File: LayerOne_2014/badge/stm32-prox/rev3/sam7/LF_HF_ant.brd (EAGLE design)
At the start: 99 x 50 mm, 30 parts

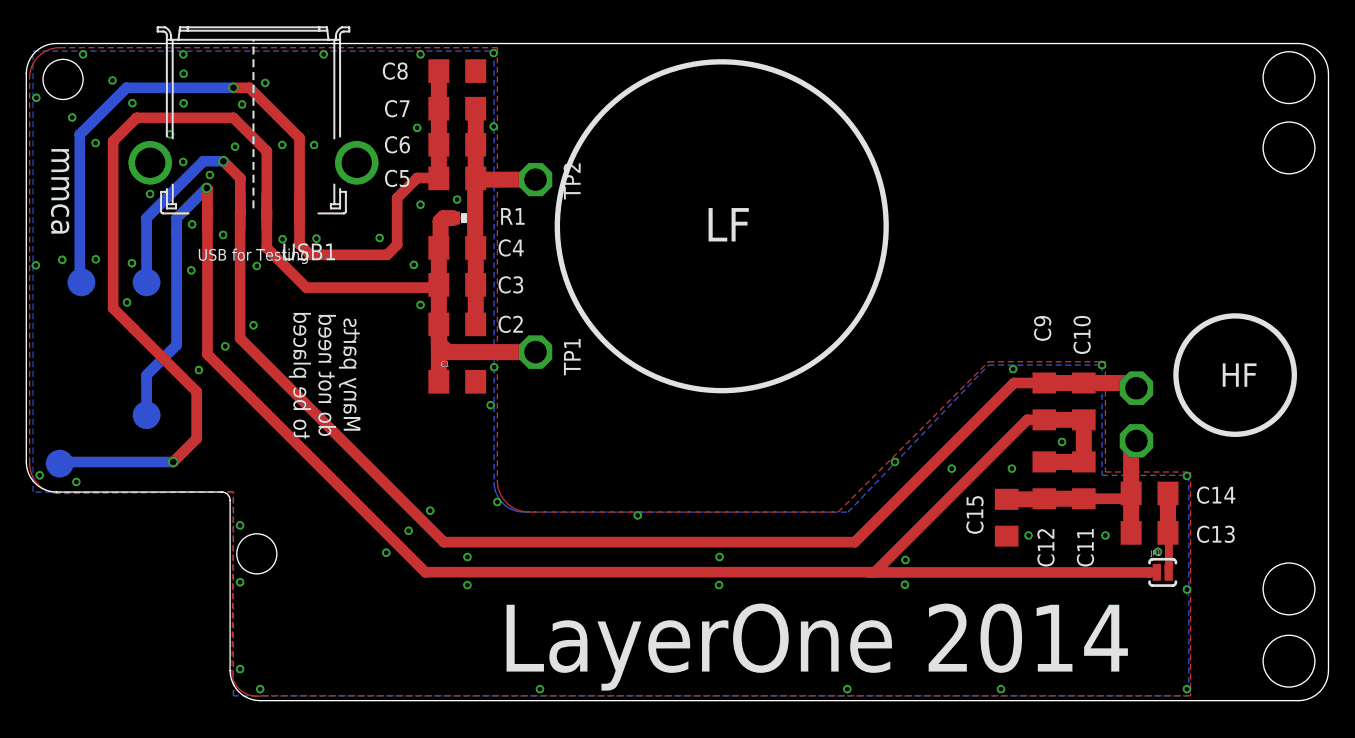
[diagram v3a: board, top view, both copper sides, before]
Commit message: 
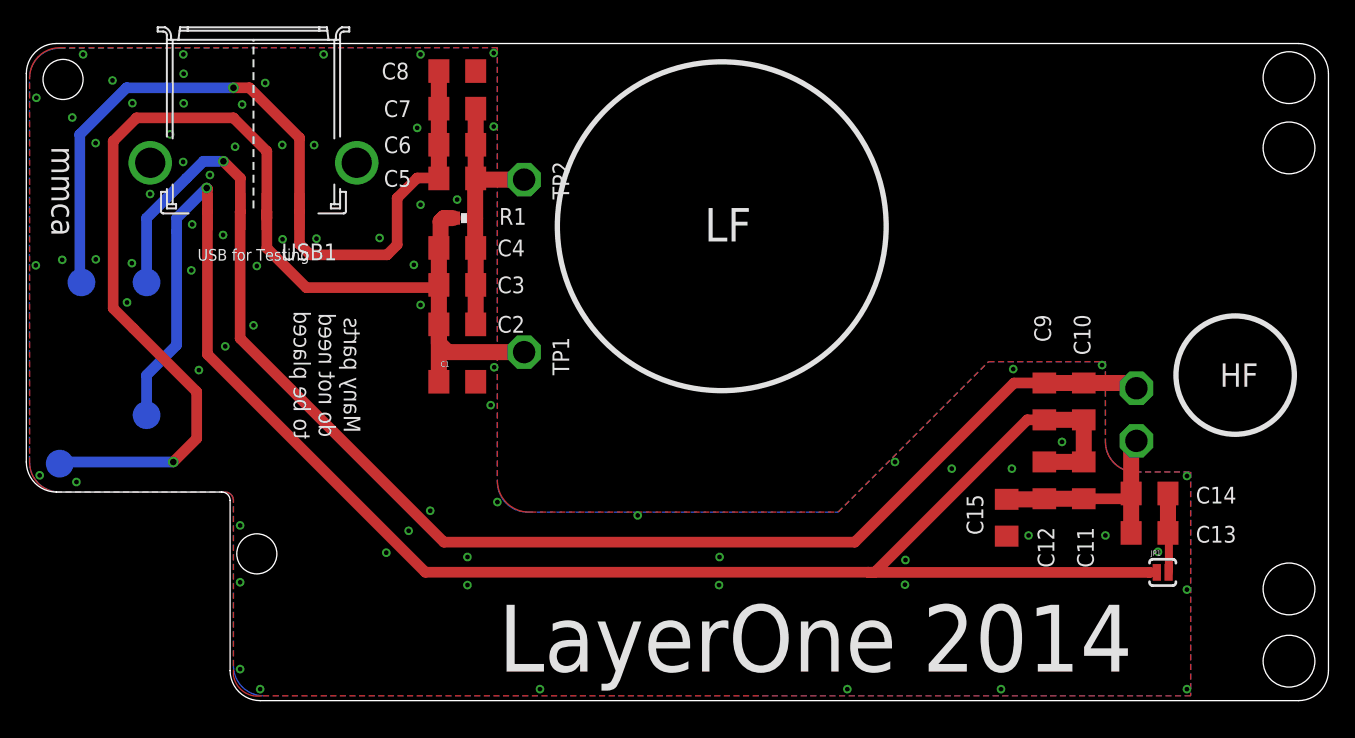
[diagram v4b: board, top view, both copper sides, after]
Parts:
- moved TP1 0.87 mm to (37.8, 1.75)
- moved TP2 0.87 mm to (37.8, 14.9)
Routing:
- net LO1: track 95.4 -> 94.5 mm
- net N$3: track 21.6 -> 20.7 mm
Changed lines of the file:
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@@
 <attribute name="VALUE" x="31.369" y="18.732" size="0.4064" layer="27"/>
 </element>
-<element name="TP1" library="testpad" package="P1-17" value="PTR1PAD1-17" x="38.716" y="1.748" smashed="yes" rot="R270">
-<attribute name="TP_SIGNAL_NAME" value="" x="35.541" y="3.018" size="1" layer="37" rot="R270"/>
-<attribute name="NAME" x="40.875" y="2.891" size="1.27" layer="25" ratio="10" rot="R270"/>
-<attribute name="VALUE" x="38.716" y="1.748" size="0.0254" layer="27" rot="R270"/>
-</element>
-<element name="TP2" library="testpad" package="P1-17" value="PTR1PAD1-17" x="38.716" y="14.86" smashed="yes" rot="R270">
-<attribute name="TP_SIGNAL_NAME" value="" x="35.541" y="16.13" size="1" layer="37" rot="R270"/>
-<attribute name="NAME" x="40.875" y="16.257" size="1.27" layer="25" ratio="10" rot="R270"/>
-<attribute name="VALUE" x="38.716" y="14.86" size="0.0254" layer="27" rot="R270"/>
+<element name="TP1" library="testpad" package="P1-17" value="PTR1PAD1-17" x="37.846" y="1.748" smashed="yes" rot="R270">
+<attribute name="TP_SIGNAL_NAME" value="" x="34.671" y="3.018" size="1" layer="37" rot="R270"/>
+<attribute name="NAME" x="40.005" y="2.891" size="1.27" layer="25" ratio="10" rot="R270"/>
+<attribute name="VALUE" x="37.846" y="1.748" size="0.0254" layer="27" rot="R270"/>
+</element>
+<element name="TP2" library="testpad" package="P1-17" value="PTR1PAD1-17" x="37.846" y="14.86" smashed="yes" rot="R270">
+<attribute name="TP_SIGNAL_NAME" value="" x="34.671" y="16.13" size="1" layer="37" rot="R270"/>
+<attribute name="NAME" x="40.005" y="16.257" size="1.27" layer="25" ratio="10" rot="R270"/>
+<attribute name="VALUE" x="37.846" y="14.86" size="0.0254" layer="27" rot="R270"/>
 </element>
 <element name="TP3" library="testpad" package="TP_MILLMAX_R" value="TP" x="2.54" y="-6.731" smashed="yes" rot="MR0">
@@
 <wire x1="18.288" y1="17.018" x2="18.288" y2="11.938" width="0.8128" layer="1"/>
 <wire x1="31.366" y1="3.858" x2="31.496" y2="3.818" width="0.8128" layer="1"/>
-<wire x1="32.034" y1="1.748" x2="38.716" y2="1.748" width="1.2192" layer="1"/>
+<wire x1="32.034" y1="1.748" x2="37.846" y2="1.748" width="1.2192" layer="1"/>
 <wire x1="8.128" y1="3.556" x2="12.954" y2="-1.27" width="0.8128" layer="1"/>
 <wire x1="12.954" y1="-1.27" x2="12.954" y2="-4.826" width="0.8128" layer="1"/>
@@
 <wire x1="34.336" y1="14.954" x2="34.166" y2="14.954" width="1.2192" layer="1"/>
 <wire x1="34.336" y1="14.954" x2="34.336" y2="14.86" width="1.2192" layer="1"/>
-<wire x1="34.336" y1="14.86" x2="38.716" y2="14.86" width="1.2192" layer="1"/>
+<wire x1="34.336" y1="14.86" x2="37.846" y2="14.86" width="1.2192" layer="1"/>
 <wire x1="34.124" y1="9.668" x2="34.166" y2="9.668" width="0.8128" layer="1"/>
 <wire x1="34.336" y1="9.572" x2="34.166" y2="9.668" width="0.8128" layer="1"/>
@@
 <signal name="GND">
 <polygon width="0.4064" layer="1">
-<vertex x="15.748" y="-8.89"/>
-<vertex x="2.5587375" y="-8.998109375" curve="-90.468374"/>
+<vertex x="15.748" y="-22.8492"/>
+<vertex x="15.748" y="-9.525" curve="90"/>
+<vertex x="15.113" y="-8.89"/>
+<vertex x="2.5587375" y="-8.89" curve="-90.468374"/>
 <vertex x="0.254" y="-6.712184375"/>
 <vertex x="0.254" y="22.606" curve="-90"/>
@@
 <vertex x="73.152" y="1.016"/>
 <vertex x="82.042" y="1.016"/>
-<vertex x="82.042" y="-7.366"/>
+<vertex x="82.042" y="-5.08" curve="90"/>
+<vertex x="84.328" y="-7.366"/>
 <vertex x="88.519" y="-7.366"/>
 <vertex x="88.519" y="-24.38398125"/>
 <vertex x="17.9179375" y="-24.384" curve="-90.274054"/>
-<vertex x="15.63894375" y="-22.8492"/>
 </polygon>
 <contactref element="C15" pad="2"/>
@@
 <via x="29.718" y="18.796" extent="1-16" drill="0.3556"/>
 <via x="35.5346" y="18.8976" extent="1-16" drill="0.3556"/>
-<polygon width="0.8128" layer="16">
-<vertex x="0.508" y="24.638"/>
-<vertex x="35.56" y="24.638"/>
-<vertex x="35.56" y="-8.128" curve="90"/>
-<vertex x="37.846" y="-10.414"/>
-<vertex x="62.484" y="-10.414"/>
-<vertex x="73.152" y="0.762"/>
-<vertex x="81.788" y="0.762"/>
-<vertex x="81.788" y="-7.62"/>
-<vertex x="88.392" y="-7.62"/>
-<vertex x="88.392" y="-24.384"/>
-<vertex x="15.748" y="-24.384"/>
-<vertex x="15.748" y="-8.89"/>
-<vertex x="0.508" y="-8.89"/>
+<polygon width="0.4064" layer="16">
+<vertex x="0.2413" y="-6.604"/>
+<vertex x="0.2413" y="22.570346875" curve="-89.938672"/>
+<vertex x="2.524853125" y="24.856346875"/>
+<vertex x="35.814" y="24.892"/>
+<vertex x="35.814" y="-8.128" curve="90"/>
+<vertex x="38.1" y="-10.414"/>
+<vertex x="61.722" y="-10.414"/>
+<vertex x="73.152" y="1.016"/>
+<vertex x="82.042" y="1.016"/>
+<vertex x="82.042" y="-5.075521875" curve="90.11216"/>
+<vertex x="84.332475" y="-7.36151875"/>
+<vertex x="88.5317" y="-7.3533"/>
+<vertex x="88.5317" y="-24.3713"/>
+<vertex x="18.0344" y="-24.3836" curve="-89.84959"/>
+<vertex x="15.748" y="-22.0976"/>
+<vertex x="15.748" y="-9.525" curve="90"/>
+<vertex x="15.113" y="-8.89"/>
+<vertex x="2.5273" y="-8.89" curve="-90"/>
 </polygon>
 <via x="88.2396" y="-23.876" extent="1-16" drill="0.3556"/>

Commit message: 
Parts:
- moved U$1 10.5 mm to (49.5, -9.40)
- moved U$2 10.5 mm to (49.5, -9.40)
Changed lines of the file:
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@@
 <layer number="22" name="bPlace" color="7" fill="1" visible="yes" active="yes"/>
 <layer number="23" name="tOrigins" color="15" fill="1" visible="yes" active="yes"/>
-<layer number="24" name="bOrigins" color="15" fill="1" visible="no" active="yes"/>
+<layer number="24" name="bOrigins" color="15" fill="1" visible="yes" active="yes"/>
 <layer number="25" name="tNames" color="7" fill="1" visible="no" active="yes"/>
 <layer number="26" name="bNames" color="7" fill="1" visible="no" active="yes"/>
@@
 <layer number="42" name="bRestrict" color="1" fill="10" visible="no" active="yes"/>
 <layer number="43" name="vRestrict" color="2" fill="10" visible="no" active="yes"/>
-<layer number="44" name="Drills" color="7" fill="1" visible="no" active="yes"/>
-<layer number="45" name="Holes" color="7" fill="1" visible="no" active="yes"/>
+<layer number="44" name="Drills" color="7" fill="1" visible="yes" active="yes"/>
+<layer number="45" name="Holes" color="7" fill="1" visible="yes" active="yes"/>
 <layer number="46" name="Milling" color="3" fill="1" visible="no" active="yes"/>
 <layer number="47" name="Measures" color="7" fill="1" visible="no" active="yes"/>
@@
 <text x="92.202" y="0" size="1.778" layer="21" font="vector" align="center">HF</text>
 <text x="53.34" y="11.43" size="2.54" layer="21" font="vector" rot="SR0" align="center">LF</text>
-<text x="60" y="-20" size="5.08" layer="21" font="vector" ratio="12" align="center">LayerOne 2014</text>
-<text x="60" y="-20.066" size="3.81" layer="22" font="vector" ratio="12" rot="MR0" align="center">layerone.org</text>
-<text x="54.102" y="21.082" size="3.175" layer="22" font="vector" ratio="12" rot="MR0" align="center">nullspacelabs.com</text>
+<text x="49.53" y="-20" size="5.08" layer="21" font="vector" ratio="12" align="center">LayerOne 2014</text>
+<text x="49.53" y="-20.066" size="3.81" layer="22" font="vector" ratio="12" rot="MR0" align="center">layerone.org</text>
+<text x="49.53" y="21.082" size="3.175" layer="22" font="vector" ratio="12" rot="MR0" align="center">nullspacelabs.com</text>
 <hole x="96" y="22.616" drill="3.937"/>
 <hole x="96" y="-21.749" drill="3.937"/>
@@
 <attribute name="VALUE" x="85.49" y="-16.651" size="0.4064" layer="27"/>
 </element>
-<element name="U$1" library="lf-antenna-usb" package="STM32-PROX_L1LOGO" value="" x="60" y="-9.398"/>
-<element name="U$2" library="lf-antenna-usb" package="STM32-PROX_L1LOGO" value="" x="60" y="-9.398" rot="MR0"/>
+<element name="U$1" library="lf-antenna-usb" package="STM32-PROX_L1LOGO" value="" x="49.53" y="-9.398"/>
+<element name="U$2" library="lf-antenna-usb" package="STM32-PROX_L1LOGO" value="" x="49.53" y="-9.398" rot="MR0"/>
 <element name="U$3" library="STM32-PROX" package="STAND-OFF-TIGHT" value="" x="2.794" y="22.479"/>
 <element name="U$4" library="STM32-PROX" package="STAND-OFF-TIGHT" value="" x="17.526" y="-13.589"/>
@@
 <via x="88.2396" y="-7.6708" extent="1-16" drill="0.3556"/>
 <via x="35.814" y="-9.652" extent="1-16" drill="0.3556"/>
-<via x="46.482" y="-10.668" extent="1-16" drill="0.3556"/>
+<via x="43.434" y="-10.668" extent="1-16" drill="0.3556"/>
 <via x="66.04" y="-6.604" extent="1-16" drill="0.3556"/>
 <via x="66.8401" y="-14.0589" extent="1-16" drill="0.3556"/>
 <via x="86.0425" y="-13.4366" extent="1-16" drill="0.3556"/>
 <via x="70.358" y="-7.112" extent="1-16" drill="0.3556"/>
-<via x="52.705" y="-13.8303" extent="1-16" drill="0.3556"/>
+<via x="54.483" y="-13.8303" extent="1-16" drill="0.3556"/>
 <via x="33.5407" y="-13.8303" extent="1-16" drill="0.3556"/>
 <via x="29.0703" y="-11.8364" extent="1-16" drill="0.3556"/>
@@
 <via x="26.8605" y="10.4267" extent="1-16" drill="0.3556"/>
 <via x="0.7239" y="8.3439" extent="1-16" drill="0.3556"/>
-<via x="66.802" y="-15.9385" extent="1-16" drill="0.3556"/>
-<via x="52.6669" y="-15.9639" extent="1-16" drill="0.3556"/>
+<via x="66.802" y="-15.9639" extent="1-16" drill="0.3556"/>
+<via x="54.4449" y="-15.9639" extent="1-16" drill="0.3556"/>
 <via x="33.5407" y="-15.9639" extent="1-16" drill="0.3556"/>
 <via x="27.3685" y="-13.5001" extent="1-16" drill="0.3556"/>
